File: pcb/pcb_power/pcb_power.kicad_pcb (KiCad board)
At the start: 2 copper layers, 100 x 79 mm, 25 parts, among them J10 JST_B4B-XH-A, J11 JST_B4P-VH, J12 XT30, K20 FINDER-40.41, K21 FINDER-40.41, Q40 BD249C, Q41 BD139, Q42 BD249C, Q43 BD139

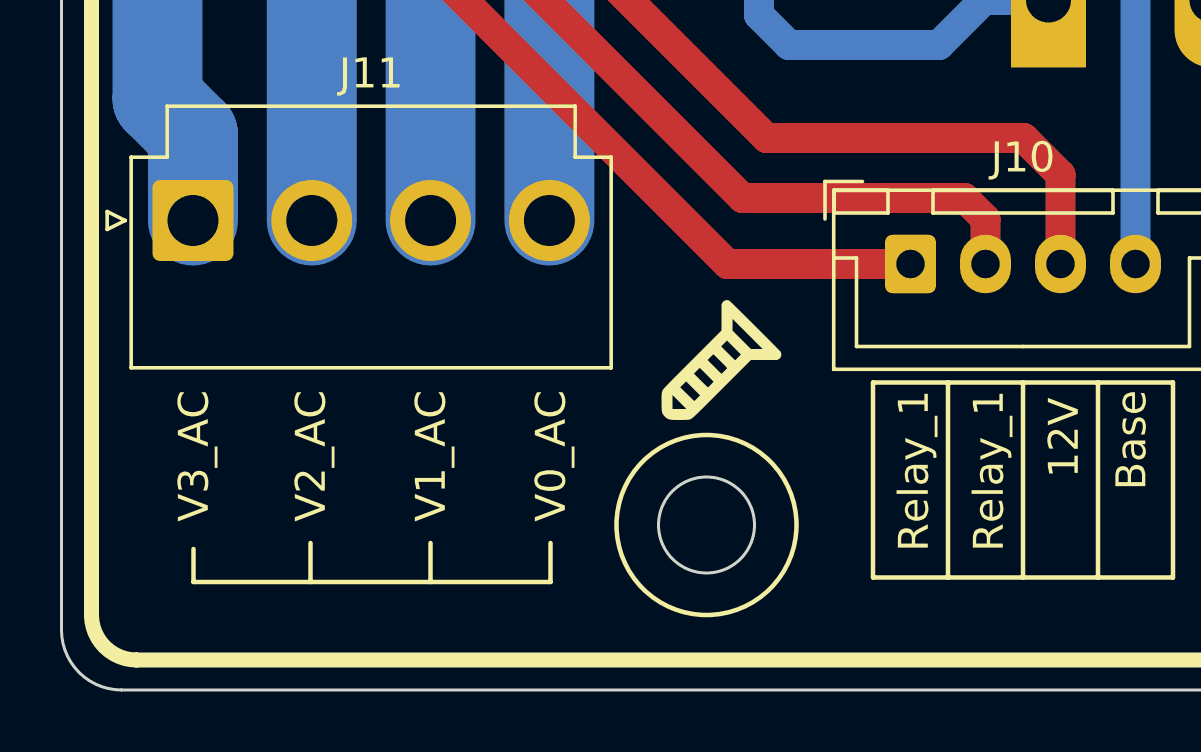
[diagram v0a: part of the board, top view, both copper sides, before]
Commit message: adjust emiter resistors values, correct relay2 silkscreen, add gerbers
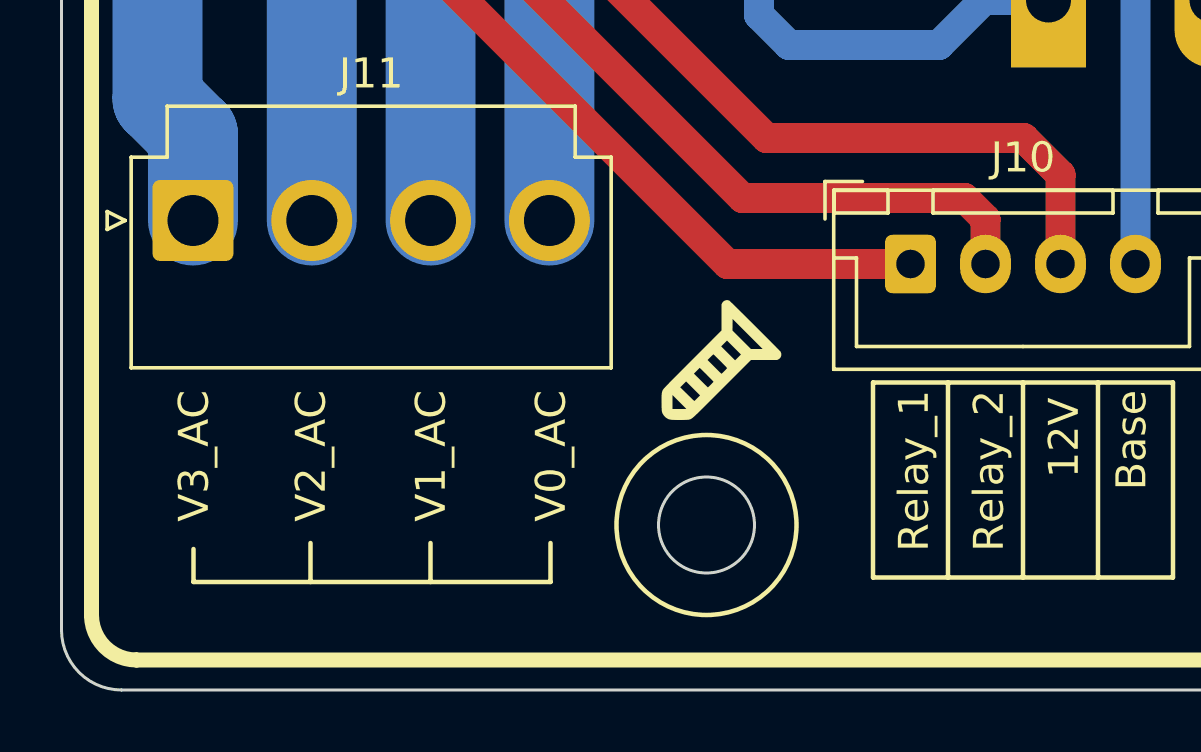
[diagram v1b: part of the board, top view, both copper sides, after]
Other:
- board text added: "Relay_2"
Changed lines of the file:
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@@
 			(plot_on_all_layers_selection 0x0000000_00000000)
 			(disableapertmacros no)
-			(usegerberextensions no)
+			(usegerberextensions yes)
 			(usegerberattributes yes)
 			(usegerberadvancedattributes yes)
-			(creategerberjobfile yes)
+			(creategerberjobfile no)
 			(dashed_line_dash_ratio 12.000000)
 			(dashed_line_gap_ratio 3.000000)
@@
 			(psnegative no)
 			(psa4output no)
-			(plotreference yes)
-			(plotvalue yes)
-			(plotfptext yes)
+			(plotreference no)
+			(plotvalue no)
+			(plotfptext no)
 			(plotinvisibletext no)
 			(sketchpadsonfab no)
-			(subtractmaskfromsilk no)
+			(subtractmaskfromsilk yes)
 			(outputformat 1)
 			(mirror no)
-			(drillshape 1)
+			(drillshape 0)
 			(scaleselection 1)
-			(outputdirectory "")
+			(outputdirectory "C:/Users/Dominik/Downloads/fab/")
 		)
 	)
@@
 			(layers "*.Cu" "*.Mask")
 			(remove_unused_layers no)
-			(roundrect_rratio 0.147059)
+			(roundrect_rratio 0.1470588235)
 			(net 6 "/Tab selector/Relay1")
 			(pinfunction "Pin_1")
@@
 			(layers "*.Cu" "*.Mask")
 			(remove_unused_layers no)
-			(roundrect_rratio 0.092593)
+			(roundrect_rratio 0.09259296296)
 			(net 10 "/Tab selector/30V_AC")
 			(pinfunction "Pin_1")
@@
 		)
 	)
-	(gr_text "Relay_1"
+	(gr_text "Relay_2"
 		(at 87.5 88.5 90)
 		(layer "F.SilkS")
